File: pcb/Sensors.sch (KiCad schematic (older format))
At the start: 7 parts

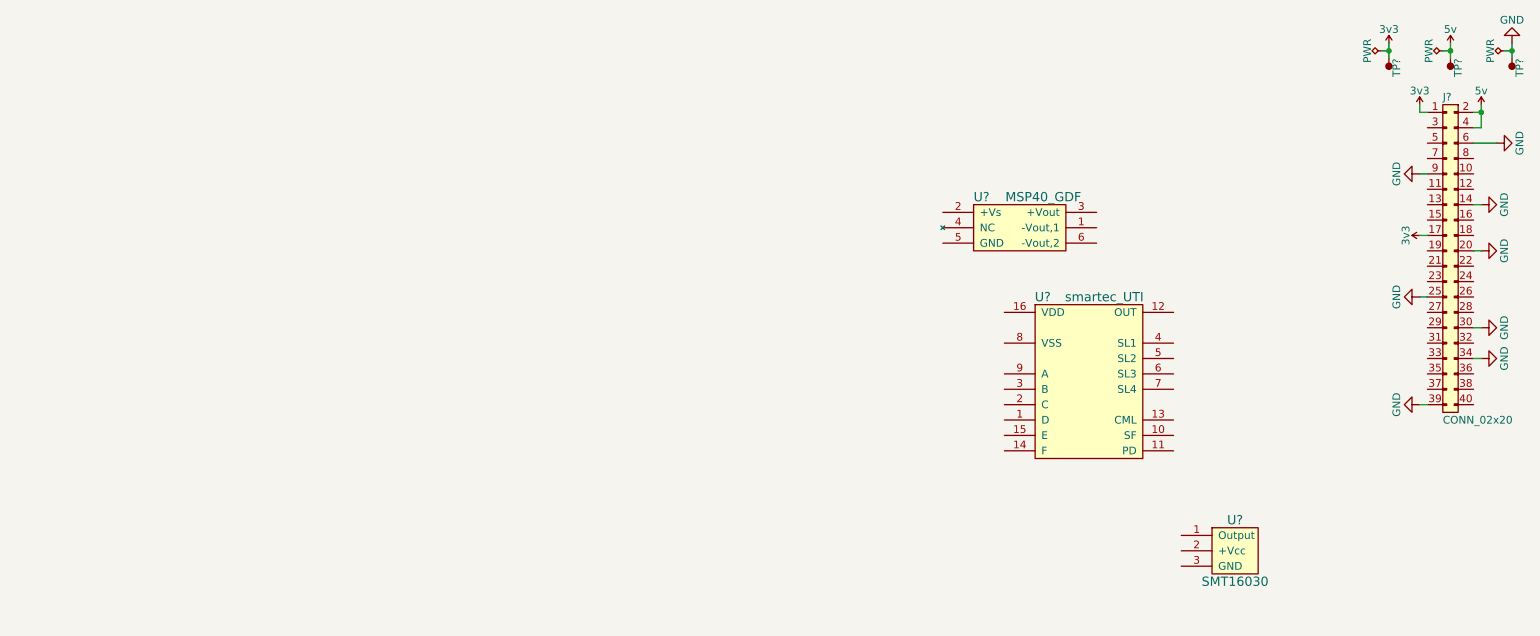
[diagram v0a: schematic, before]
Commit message: Add to schematic and footprints
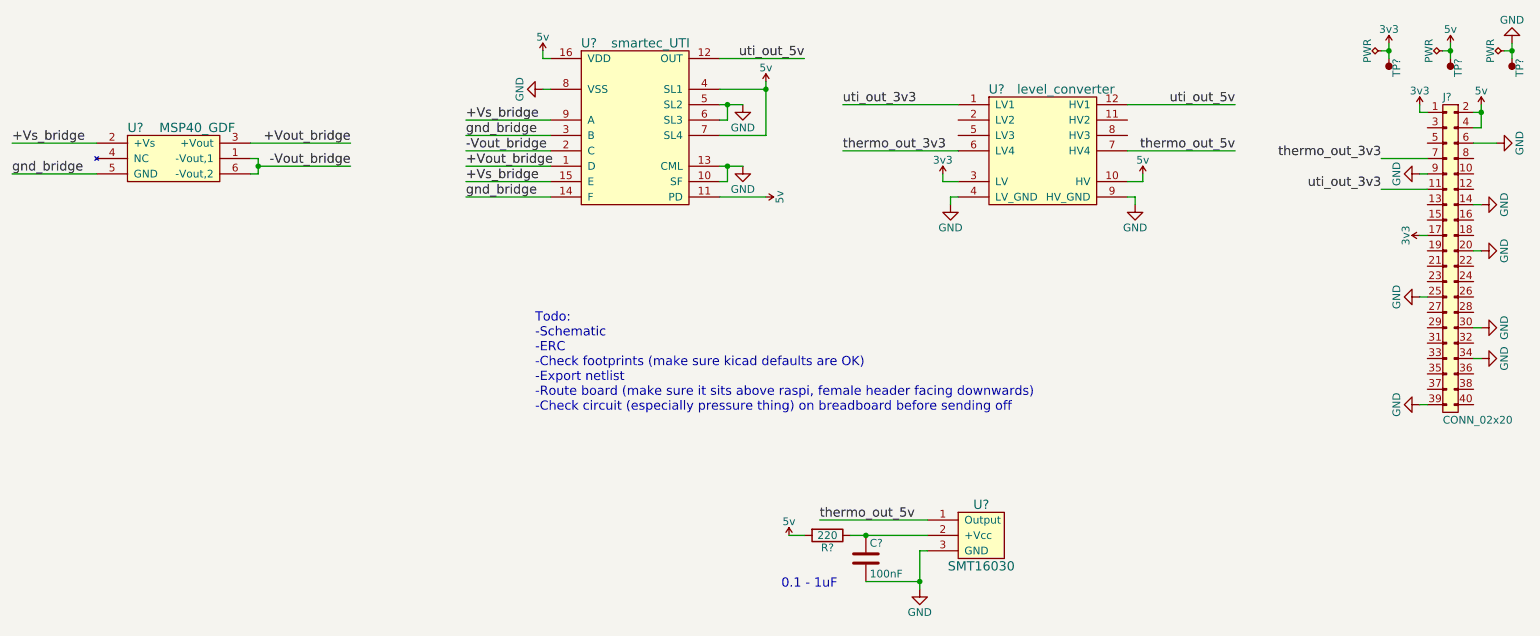
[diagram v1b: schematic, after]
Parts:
- added C?: 100nF, symbol C
- added R?: 220, symbol R
- added U?: level_converter, Sensors:Level_converter, symbol level_converter
- U?: footprint (none) -> Sensors:MSP40_GDF
- U?: footprint (none) -> Sensors:DIP-16_W7.62mm_LongPads; Farnell (none) -> Value
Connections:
- net 3v3: now also U?.3 (LV)
- net 5v: now also U?.11 (PD), U?.16 (VDD), U?.4 (SL1), U?.7 (SL4), R?.2, U?.10 (HV)
- net GND: now also U?.10 (SF), U?.13 (CML), U?.3 (GND), U?.5 (SL2), U?.6 (SL3), U?.8 (VSS), C?.2, U?.4 (LV_GND), U?.9 (HV_GND)
- net -Vout_bridge: now reaches U?.1 (-Vout,1)
- net -Vout_bridge: now also U?.2 (C), U?.6 (-Vout,2)
- net +Vs_bridge: now reaches U?.2 (+Vs)
- net +Vs_bridge: now also U?.15 (E), U?.9 (A)
- net +Vout_bridge: now reaches U?.3 (+Vout)
- net +Vout_bridge: now also U?.1 (D)
- net gnd_bridge: now reaches U?.5 (GND)
- net gnd_bridge: now also U?.14 (F), U?.3 (B)
- net uti_out_3v3: now reaches J?.11
- net uti_out_3v3: now also U?.1 (LV1)
- net thermo_out_3v3: now reaches J?.7
- net thermo_out_3v3: now also U?.6 (LV4)
- net uti_out_5v: now reaches U?.12 (OUT)
- net uti_out_5v: now also U?.12 (HV1)
- net thermo_out_5v: now reaches U?.1 (Output)
- net thermo_out_5v: now also U?.7 (HV4)
- net at U?.2 (+Vcc): now also C?.1, R?.1
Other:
- note added: "0.1 - 1uF"
- note added: "Todo:\n-Schematic\n-ERC\n-Check footprints (make sure kicad defaults are OK)\n-Export netlist\n-Route board (make sure it sits above raspi, female header facing downwards)\n-Check circuit (especially pressure thing) on breadboard before sending off"
- moved on the sheet: U?

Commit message: Route PCB
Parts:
- C1: renamed from C?; footprint (none) -> Sensors:rectangular_capacitor_5mm_pitch
- R1: renamed from R?; footprint (none) -> Resistors_ThroughHole:Resistor_Horizontal_RM15mm
- TP1, TP2, TP3: renamed from TP?; footprint agg:TESTPAD -> Sensors:TESTPAD_3mm; Farnell (none) -> Value
- gave numbers to parts that had none: 5
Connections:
- no-connect marks 0 -> 32
